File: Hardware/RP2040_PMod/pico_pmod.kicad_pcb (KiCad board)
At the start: 2 copper layers, 50 x 37 mm, 45 parts, among them J1 Conn_02x06_Odd_Even, J2 Conn_02x06_Odd_Even, J3 Conn_02x06_Odd_Even, J4 USB_C_Receptacle_USB2.0, J5 Conn_01x04, SW1 SW_Push, SW2 SW_Push, U1 RP2040, U2 W25Q128JVS, U3 NCP1117-3.3_SOT223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

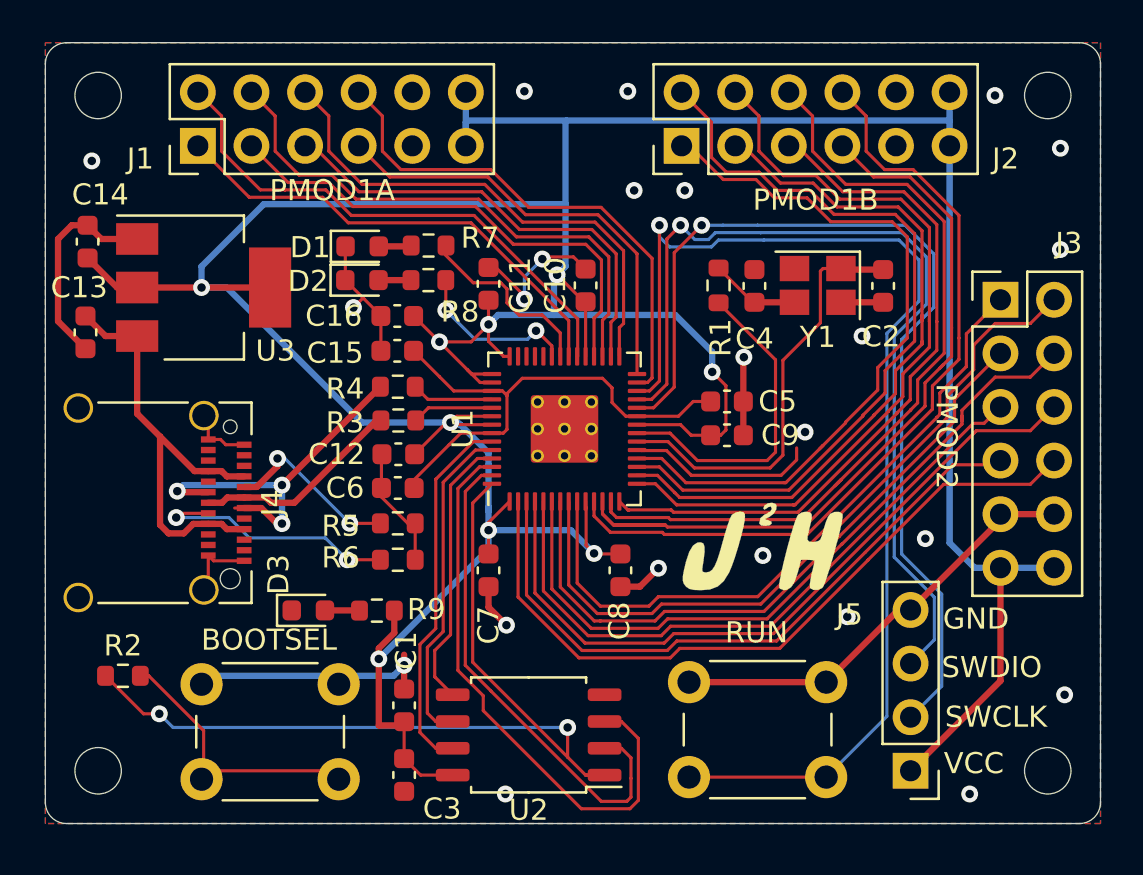
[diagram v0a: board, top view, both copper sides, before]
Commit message: Correct DRC warning for unconnected tracks and overlapping silkscreen
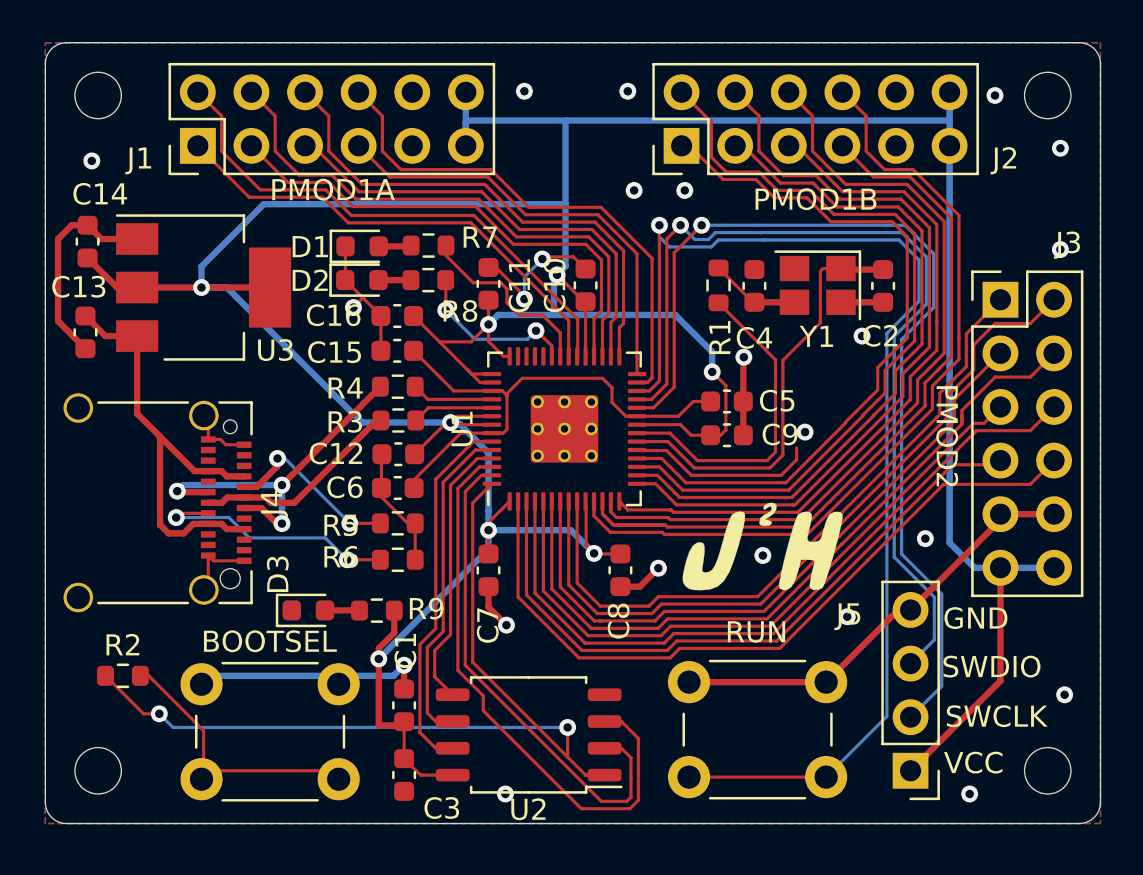
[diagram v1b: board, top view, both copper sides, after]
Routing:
- net +3V3: track 199.5 -> 198.7 mm, vias 9 -> 8
- net GPIO_10: track 38.1 -> 37.4 mm
- net GPIO_3: track 31.9 -> 31.3 mm
- net USB_DM: track 17.7 -> 17.1 mm
- net GND: track 87.4 -> 86.8 mm
